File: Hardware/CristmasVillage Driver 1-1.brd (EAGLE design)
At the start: 94.2 x 41.8 mm, 53 parts, among them CN1 MJ-180SMT, CN2-PROG JST-6PSPI-SIDE-S6B, CN3-SERIAL JST-4PSIDE-S4B, CN5-LEDSTRIPS HDR_2X10_SIDE-MOUNT, IC1 UA78M05DCY, IC2 LM358D, IC3 LM358D, IC4 LM358D, IC5 ATTINY-4/5/9/10, IC6 TINY2313-*S*, Q1 Si2309CD, Q10 NX7002AKW, Q11 NX7002AKW, Q12 NX7002AKW, Q2 NX7002AKW, Q3 NX7002AKW, Q4 NX7002AKW, Q5 NX7002AKW, Q6 NX7002AKW, Q7 NX7002AKW, Q8 NX7002AKW, Q9 NX7002AKW, SW1 POWER, SW2 NIGHT-MODE

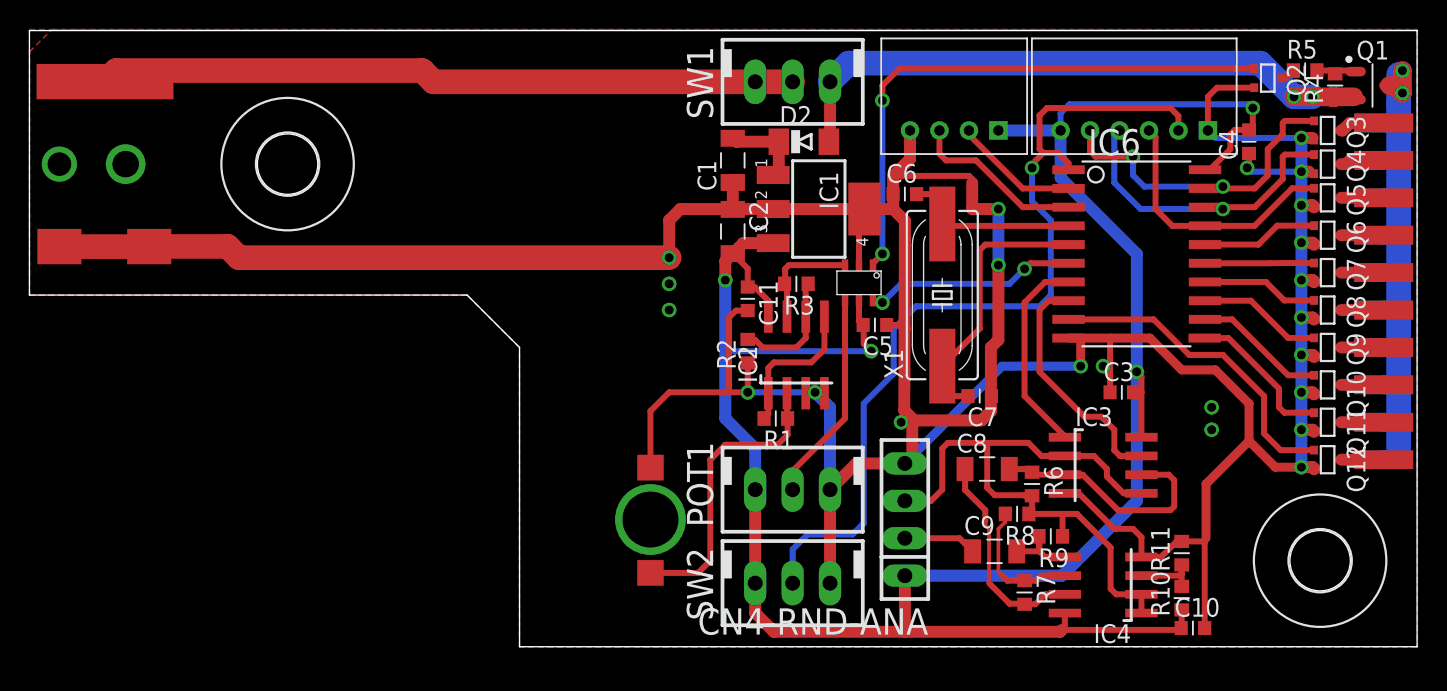
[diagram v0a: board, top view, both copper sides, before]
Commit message: Changed from FM tuned antenna idea to Zener Noise for random: v1.1
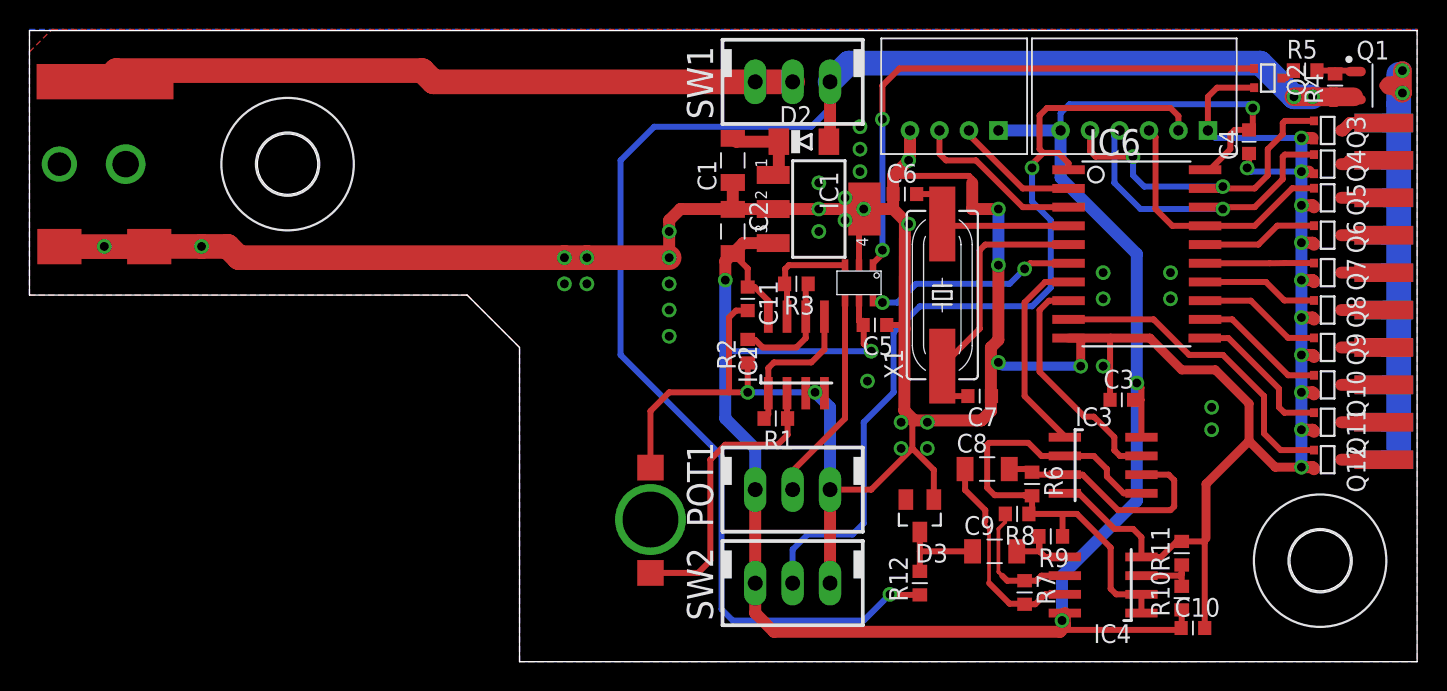
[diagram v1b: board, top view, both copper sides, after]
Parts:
- removed CN4-RND-ANA: (no value), con-hdrs40:SIP-100-4V
- added D3: 9V1, diode:SOT23
- added R12: 1M, ipc-7351-resistor:RESC1608X55N
- C8, C9: value (none) -> 1u
- R1: value (none) -> 1M
- R2: value (none) -> 10k
- R3: value (none) -> 490k
- R7: value (none) -> 99k
- R8: value (none) -> 1k
- R9: value 1M -> 500k
- moved C3 0.51 mm to (125.2, 45.7)
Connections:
- removed net RANDOM-ANALOG-SIG: C9.1, CN4-RND-ANA.2
- new net N$42: C9.1, D3.3, R12.2
- net +12V: now also R12.1
- net GND: now also D3.1; no longer CN4-RND-ANA.4
- net HALF-VCC: no longer CN4-RND-ANA.3
- net V+: no longer CN4-RND-ANA.1
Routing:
- net +12V: track 42.7 -> 108.0 mm, vias 2 -> 3
- net V+: track 159.5 -> 148.5 mm, vias 4 -> 5
- net HALF-VCC: track 43.1 -> 34.1 mm
- net N$42: track 0.00 -> 6.25 mm
- net GND: track 282.0 -> 277.0 mm, vias 23 -> 51
- net RANDOM-ANALOG-SIG: track 4.96 -> 0.00 mm
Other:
- board size 94.2 x 41.8 mm -> 94.2 x 42.9 mm
